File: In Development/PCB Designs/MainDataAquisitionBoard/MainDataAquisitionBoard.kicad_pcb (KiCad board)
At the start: 2 copper layers, 120.7 x 83.8 mm, 23 parts, among them J1 Conn_01x08, J10 3v3, J11 TopR, J12 TopL, J13 BottomR, J14 BottomL, J15 RTC, J16 XbeeL, J17 XbeeR, J18 Conn_02x03_Counter_Clockwise, J19 Power in, J2 Conn_01x08, J3 GND, J4 1x24, J5 Teensy 3.6L, J6 Teensy 3.6R, J7 1x24, J8 5V, J9 Conn_01x04

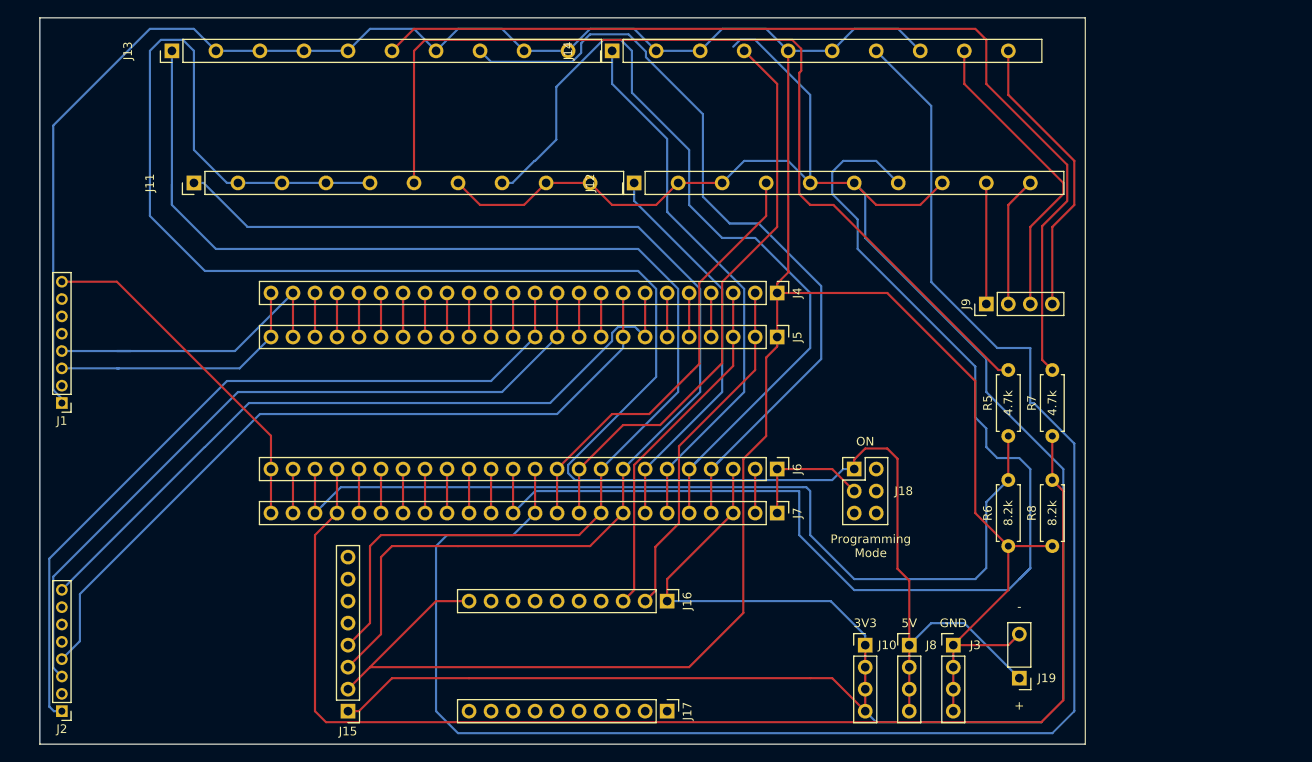
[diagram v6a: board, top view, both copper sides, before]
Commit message: Finished DAQ and eCVT PCBs rev 2.1. Ready for ordering from JLCPCB
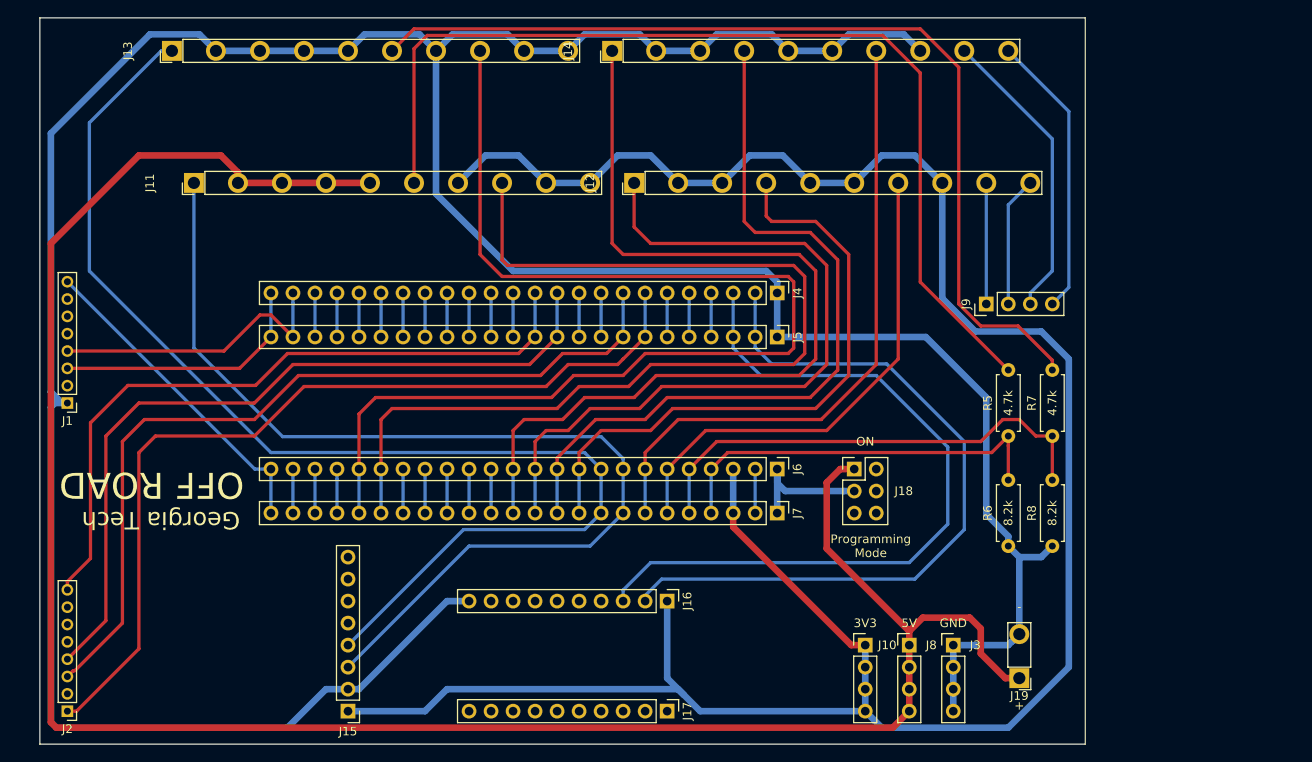
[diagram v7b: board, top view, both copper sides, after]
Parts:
- moved J1 0.63 mm to (66.7, 95.2)
- moved J2 0.63 mm to (66.7, 130.8)
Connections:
- J4 pad 11: Net-(J2-Pad3) -> Net-(J2-Pad4)
- J4 pad 12: Net-(J2-Pad1) -> Net-(J2-Pad8)
- J4 pad 7: Net-(J2-Pad8) -> Net-(J2-Pad1)
- J4 pad 8: Net-(J2-Pad4) -> Net-(J2-Pad3)
- J5 pad 11: Net-(J2-Pad3) -> Net-(J2-Pad4)
- J5 pad 12: Net-(J2-Pad1) -> Net-(J2-Pad8)
- J5 pad 7: Net-(J2-Pad8) -> Net-(J2-Pad1)
- J5 pad 8: Net-(J2-Pad4) -> Net-(J2-Pad3)
- J6 pad 10: Net-(J14-Pad4) -> Net-(J12-Pad4)
- J6 pad 11: Net-(J12-Pad4) -> Net-(J14-Pad4)
- J6 pad 12: Net-(J14-Pad7) -> Net-(J12-Pad1)
- J6 pad 13: Net-(J12-Pad7) -> Net-(J14-Pad1)
- J6 pad 19: Net-(J6-Pad19) -> Net-(J11-Pad8)
- J6 pad 20: Net-(J6-Pad20) -> Net-(J13-Pad8)
- J6 pad 4: Net-(J13-Pad8) -> Net-(J6-Pad4)
- J6 pad 5: Net-(J11-Pad8) -> Net-(J6-Pad5)
- J6 pad 6: Net-(J14-Pad1) -> Net-(J12-Pad7)
- J6 pad 7: Net-(J12-Pad1) -> Net-(J14-Pad7)
- J7 pad 10: Net-(J14-Pad4) -> Net-(J12-Pad4)
- J7 pad 11: Net-(J12-Pad4) -> Net-(J14-Pad4)
- J7 pad 12: Net-(J14-Pad7) -> Net-(J12-Pad1)
- J7 pad 13: Net-(J12-Pad7) -> Net-(J14-Pad1)
- J7 pad 19: Net-(J6-Pad19) -> Net-(J11-Pad8)
- J7 pad 20: Net-(J6-Pad20) -> Net-(J13-Pad8)
- J7 pad 4: Net-(J13-Pad8) -> Net-(J6-Pad4)
- J7 pad 5: Net-(J11-Pad8) -> Net-(J6-Pad5)
- J7 pad 6: Net-(J14-Pad1) -> Net-(J12-Pad7)
- J7 pad 7: Net-(J12-Pad1) -> Net-(J14-Pad7)
- R5 pad 1: Net-(J6-Pad22) -> Net-(J6-Pad4)
- R6 pad 2: Net-(J6-Pad22) -> Net-(J6-Pad4)
- R7 pad 1: Net-(J6-Pad21) -> Net-(J6-Pad5)
- R8 pad 2: Net-(J6-Pad21) -> Net-(J6-Pad5)
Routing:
- net Net-(J6-Pad21): track 147.9 -> 5.08 mm
- net Net-(J14-Pad7): track 201.0 -> 74.1 mm
- net Net-(J6-Pad22): track 108.0 -> 5.08 mm
- net Net-(J12-Pad7): track 142.3 -> 57.3 mm
- net Net-(J6-Pad5): track 0.00 -> 55.2 mm
- net Net-(J6-Pad4): track 0.00 -> 46.0 mm
- net Net-(J16-Pad3): track 40.8 -> 86.6 mm
- net Net-(J16-Pad2): track 40.8 -> 85.7 mm
- net Net-(J14-Pad1): track 63.3 -> 105.1 mm
- net Net-(J12-Pad1): track 46.0 -> 86.2 mm
- net Net-(J13-Pad8): track 93.2 -> 133.4 mm
- net Net-(J10-Pad1): track 294.9 -> 268.5 mm
- net Net-(J14-Pad4): track 66.9 -> 88.0 mm
- net Net-(J12-Pad4): track 50.6 -> 70.9 mm
- net Net-(J11-Pad8): track 96.7 -> 116.3 mm
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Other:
- board text added: "Georgia Tech"
- board text added: "OFF ROAD"
